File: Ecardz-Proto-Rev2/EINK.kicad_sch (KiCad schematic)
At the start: 21 parts, among them J2 Conn_01x24, Q1 NMOS

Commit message: most of layout complete
switched ADC pins for ease of layout. added LEDs
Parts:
- R2: now not fitted
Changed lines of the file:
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@@
 		(in_bom yes)
 		(on_board yes)
-		(dnp no)
+		(dnp yes)
 		(fields_autoplaced yes)
 		(property "Reference" "R2"

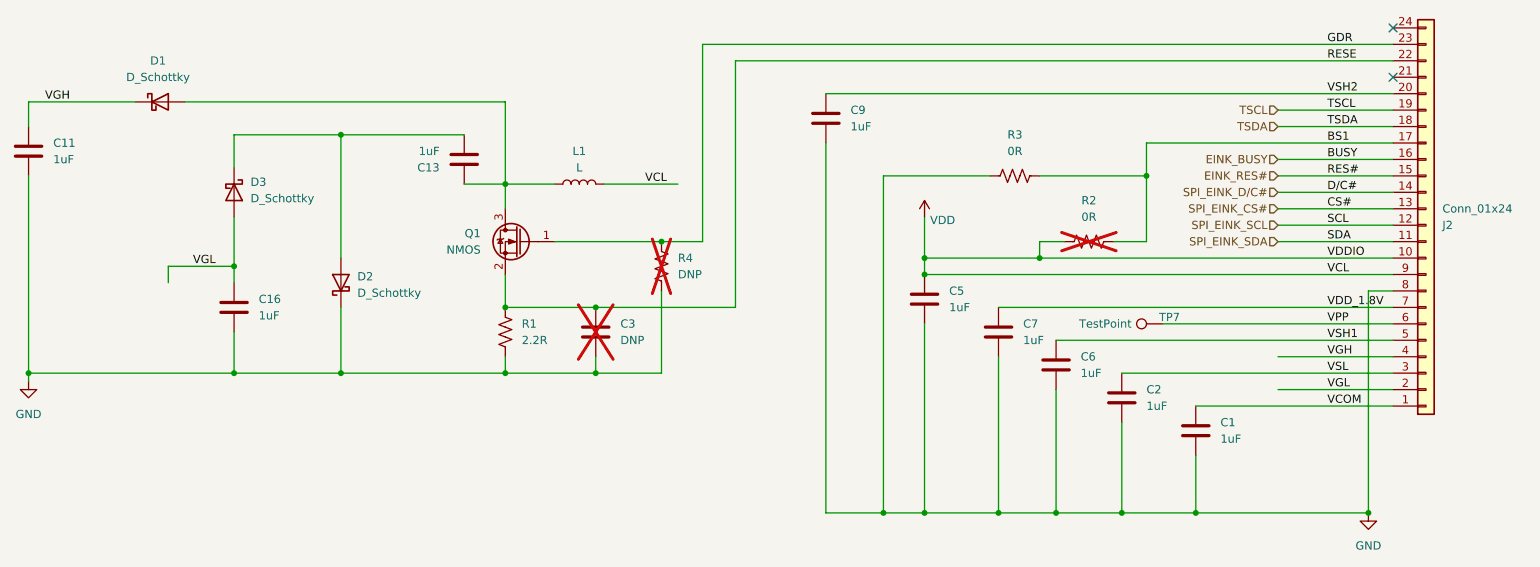
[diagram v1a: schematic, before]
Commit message: final schematic
final schematic done and BOM generated except for pogo pins and capacitors
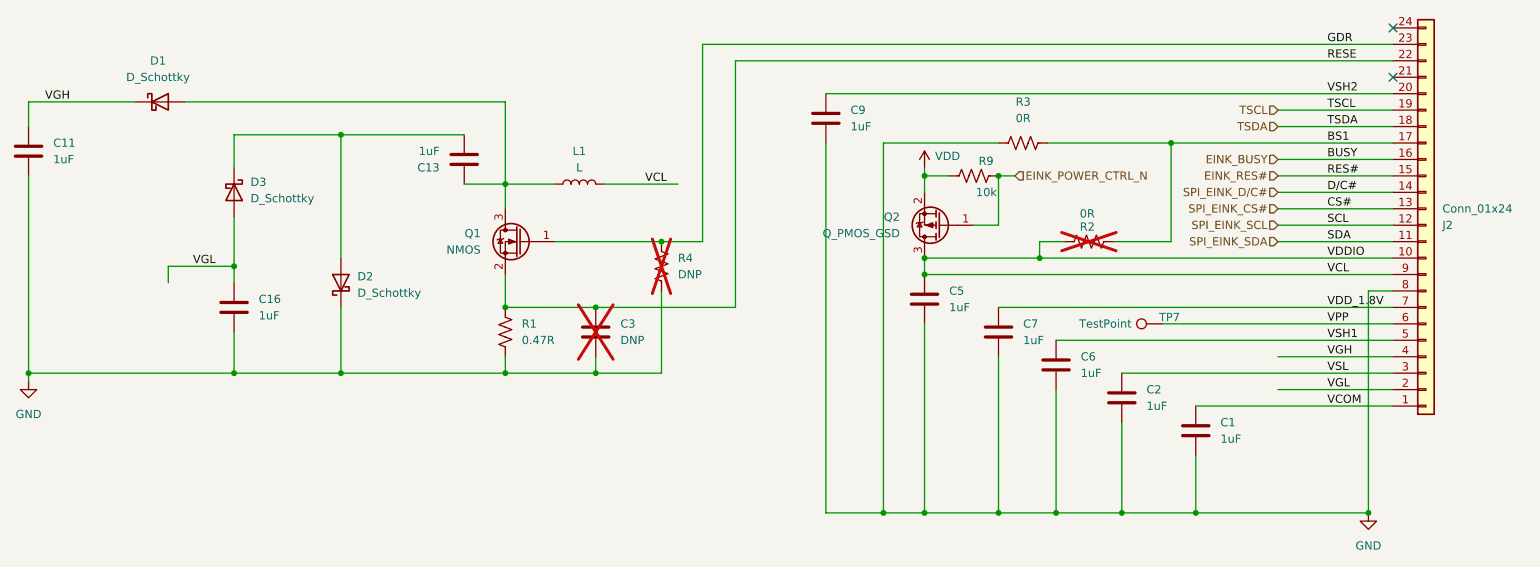
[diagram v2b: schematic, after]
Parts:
- added Q2: Q_PMOS_GSD, Package_TO_SOT_SMD:SOT-23, symbol Device:Q_PMOS_GSD
- added R9: 10k, Resistor_SMD:R_0603_1608Metric_Pad0.98x0.95mm_HandSolder, symbol Device:R_US
- R1: value 2.2R -> 0.47R; Digikey Part Number 311-2.2HRTR-ND -> ERJ-3RQJR47V; MANUFACTURER PART NUMBER RC0603FR-072R2L -> ERJ-3RQJR47V
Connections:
- net VDD: now also Q2.2 (S), R9.1; no longer C5.1, J2.10 (Pin_10), J2.9 (Pin_9), L1.2, R2.1
- new net EINK_POWER_CTRL_N: Q2.1 (G), R9.2
- new net VCL: C5.1, J2.10 (Pin_10), J2.9 (Pin_9), L1.2, Q2.3 (D), R2.1
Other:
- moved on the sheet: R3

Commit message: initial fit check for mech
final footprints defined and placement is mostly complete
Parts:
- removed TP7: TestPoint, TestPoint:TestPoint_Pad_2.0x2.0mm, symbol Connector:TestPoint
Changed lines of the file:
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@@
-		)
-	)
-	(symbol
-		(lib_id "Connector:TestPoint")
-		(at 223.52 72.39 90)
-		(unit 1)
-		(exclude_from_sim no)
-		(in_bom yes)
-		(on_board yes)
-		(dnp no)
-		(property "Reference" "TP7"
-			(at 224.536 71.374 90)
-			(effects
-				(font
-					(size 1.27 1.27)
-				)
-			)
-		)
-		(property "Value" "TestPoint"
-			(at 214.63 72.39 90)
-			(effects
-				(font
-					(size 1.27 1.27)
-				)
-			)
-		)
-		(property "Footprint" "TestPoint:TestPoint_Pad_2.0x2.0mm"
-			(at 223.52 67.31 0)
-			(effects
-				(font
-					(size 1.27 1.27)
-				)
-				(hide yes)
-			)
-		)
-		(property "Datasheet" "~"
-			(at 223.52 67.31 0)
-			(effects
-				(font
-					(size 1.27 1.27)
-				)
-				(hide yes)
-			)
-		)
-		(property "Description" "test point"
-			(at 223.52 72.39 0)
-			(effects
-				(font
-					(size 1.27 1.27)
-				)
-				(hide yes)
-			)
-		)
-		(property "Digikey Part Number" ""
-			(at 223.52 72.39 0)
-			(effects
-				(font
-					(size 1.27 1.27)
-				)
-				(hide yes)
-			)
-		)
-		(pin "1"
-		)
-		(instances
-			(project "Ecardz-Proto"
-				(path "/2adbba85-9270-4efb-857d-656bb51406ca/a8646e5d-e29c-4dc0-b052-9a424836bd67"
-					(reference "TP7")
-					(unit 1)
-				)
-			)
 		)
 	)
